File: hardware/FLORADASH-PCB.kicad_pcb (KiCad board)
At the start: 2 copper layers, 101.5 x 58.8 mm, 76 parts, among them IC1 LM66200DRLR, J1 USB_C_Receptacle_USB2.0_16P, J2 Conn_01x04_Pin, J3 Conn_02x04_Top_Bottom, Q1 FS8205, Q2 FS8205, SW1 SW_Push, SW2 SW_Push, U1 TP4056-42-ESOP8, U2 USBLC6-2SC6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

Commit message: Routing structure
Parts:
- BT1: moved to B.Cu
- L2: footprint Inductor_SMD:L_0603_1608Metric -> Inductor_SMD:L_1008_2520Metric
- TP1, TP2, TP3, TP4, TP5, TP6: footprint TestPoint:TestPoint_Pad_D2.5mm -> TestPoint:TestPoint_Pad_D1.0mm
- moved C9 181.0 mm to (104.5, 94.2), turned to -90 degrees
- moved U5 178.8 mm to (107.5, 93.8)
- moved D1 171.9 mm to (115.2, 93.7), turned to 90 degrees
- moved R1 171.7 mm to (113.5, 93.7), turned to -90 degrees
- moved IC1 170.7 mm to (111.5, 93.8), turned to 180 degrees
- moved TP3 170.6 mm to (111.8, 91.2)
- moved R13 122.7 mm to (132.0, 75.7), turned to 180 degrees
- moved Q1 122.4 mm to (116.0, 126.5)
- moved TP2 122.2 mm to (120.2, 106.5)
- moved C7 120.6 mm to (127.2, 79.5), turned to 90 degrees
- moved L2 119.7 mm to (137.5, 79.8), turned to -90 degrees
- moved TP4 118.6 mm to (107.5, 96.2)
- moved Q2 116.1 mm to (111.0, 126.5), turned to 180 degrees
- moved C6 115.3 mm to (139.8, 79.8), turned to 90 degrees
- moved U3 114.9 mm to (110.5, 122.4), turned to 90 degrees
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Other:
- board size 101.5 x 58.8 mm -> 88.8 x 45.5 mm
- copper layers 2 -> 4

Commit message: Added the soil moisture sensor on PCB
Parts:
- added G***: LOGO, SparkFun-Aesthetic:SparkFun_Logo_10mm, F.Cu at (263.2, 88.7)
- added G***: LOGO, SparkFun-Aesthetic:SparkFun_Logo_10mm, B.Cu at (263.2, 100.4)
- added kibuzzard-693B565E: G***, kibuzzard-693B565E, F.Cu at (246.7, 88.5)
- added kibuzzard-693B565E: G***, kibuzzard-693B565E, B.Cu at (246.7, 100.7)
- added kibuzzard-6969377A: G***, kibuzzard-6969377A, F.Cu at (231.0, 94.6)
- added kibuzzard-6969378A: G***, kibuzzard-6969378A, F.Cu at (236.1, 96.8)
- added kibuzzard-69693792: G***, kibuzzard-69693792, F.Cu at (242.4, 96.8)
- added kibuzzard-69693797: G***, kibuzzard-69693797, F.Cu at (248.8, 96.8)
- added kibuzzard-6969379D: G***, kibuzzard-6969379D, F.Cu at (255.1, 96.8)
- added kibuzzard-696937A1: G***, kibuzzard-696937A1, F.Cu at (261.4, 96.8)
- added kibuzzard-696937A5: G***, kibuzzard-696937A5, F.Cu at (267.8, 96.8)
- added kibuzzard-6983799B: G***, kibuzzard-6983799B, B.Cu at (231.6, 94.6)
- added kibuzzard-69837BBB: G***, kibuzzard-69837BBB, B.Cu at (270.3, 93.5)
- added kibuzzard-69837BD1: G***, kibuzzard-69837BD1, B.Cu at (265.3, 93.5)
- added kibuzzard-69837BDA: G***, kibuzzard-69837BDA, B.Cu at (260.3, 93.5)
- added kibuzzard-69837BE0: G***, kibuzzard-69837BE0, B.Cu at (255.3, 93.5)
- added kibuzzard-69837BE5: G***, kibuzzard-69837BE5, B.Cu at (250.3, 93.5)
- added kibuzzard-69837BE9: G***, kibuzzard-69837BE9, B.Cu at (245.3, 93.5)
- added kibuzzard-69837BEE: G***, kibuzzard-69837BEE, B.Cu at (240.3, 93.5)
- added kibuzzard-69837BF5: G***, kibuzzard-69837BF5, B.Cu at (235.3, 93.5)
- moved U6 112.5 mm to (201.4, 19.6)
- moved R18 49.1 mm to (131.2, -51.4)
- moved R10 48.6 mm to (62.4, 42.0), turned to 180 degrees
- moved R11 48.3 mm to (62.4, 43.9), turned to 180 degrees
- moved C5 46.1 mm to (64.8, 42.8), turned to -90 degrees
- moved R9 45.1 mm to (59.2, 41.9)
- moved D5 44.2 mm to (128.0, -51.4)
- moved C12 39.8 mm to (128.8, -54.0), turned to -90 degrees
- moved C11 37.1 mm to (130.4, -54.0), turned to -90 degrees
- moved C10 34.5 mm to (132.0, -54.0), turned to -90 degrees
- moved R21 32.4 mm to (154.6, -52.0), turned to 180 degrees
- moved R20 31.8 mm to (154.6, -53.6), turned to 180 degrees
- moved U8 26.6 mm to (142.9, -49.0)
- moved R17 24.4 mm to (154.6, -46.0)
- moved R15 18.4 mm to (154.6, -44.4)
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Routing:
- added copper zone on B.Cu, net TO_CAP_PLATE
- added copper zone on F.Cu, net TO_CAP_PLATE
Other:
- board size 88.8 x 45.5 mm -> 179.8 x 45.6 mm
- board text added: "Route Out"

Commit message: Placement of the Cap Sense
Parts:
- moved G*** 41.3 mm to (224.9, 104.1)
- moved G*** 41.3 mm to (224.9, 115.8)
- moved kibuzzard-6969377A 41.3 mm to (192.7, 110.0)
- moved kibuzzard-6969378A 41.3 mm to (197.8, 112.2)
- moved kibuzzard-69693792 41.3 mm to (204.1, 112.2)
- moved kibuzzard-69693797 41.3 mm to (210.4, 112.2)
- moved kibuzzard-6969379D 41.3 mm to (216.8, 112.2)
- moved kibuzzard-696937A5 41.3 mm to (229.5, 112.2)
- moved kibuzzard-69837BBB 41.3 mm to (232.0, 108.9)
- moved kibuzzard-69837BD1 41.3 mm to (227.0, 108.9)
- moved kibuzzard-69837BDA 41.3 mm to (222.0, 108.9)
- moved kibuzzard-693B565E 41.3 mm to (208.4, 103.9)
- moved kibuzzard-696937A1 41.3 mm to (223.2, 112.2)
- moved kibuzzard-6983799B 41.3 mm to (193.3, 110.0)
- moved kibuzzard-693B565E 41.3 mm to (208.4, 116.1)
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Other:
- board size 179.8 x 45.6 mm -> 141.4 x 44.3 mm

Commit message: Placement of components on PCB
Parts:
- U6: footprint Connector_PinSocket_2.54mm:PinSocket_1x03_P2.54mm_Vertical -> Connector_PinSocket_2.54mm:PinSocket_1x03_P2.54mm_Horizontal
- moved H3 238.2 mm to (188.2, 88.2)
- moved H4 234.4 mm to (188.4, 133.0)
- moved H1 153.6 mm to (104.2, 88.8)
- moved H2 150.3 mm to (104.2, 133.0)
- moved R9 122.4 mm to (139.6, 134.2), turned to 90 degrees
- moved C16 120.6 mm to (175.8, 105.0)
- moved D4 120.6 mm to (186.7, 106.0)
- moved C15 120.6 mm to (175.8, 106.6)
- moved C13 120.6 mm to (179.4, 109.2)
- moved C14 120.6 mm to (182.6, 109.2)
- moved R14 120.6 mm to (186.6, 104.4)
- moved R16 120.6 mm to (186.7, 107.6)
- moved U7 120.6 mm to (181.2, 105.6)
- moved R10 117.9 mm to (139.8, 131.0), turned to -90 degrees
- moved R11 117.7 mm to (141.6, 131.0), turned to -90 degrees
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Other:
- board size 141.4 x 44.3 mm -> 141.4 x 50.8 mm

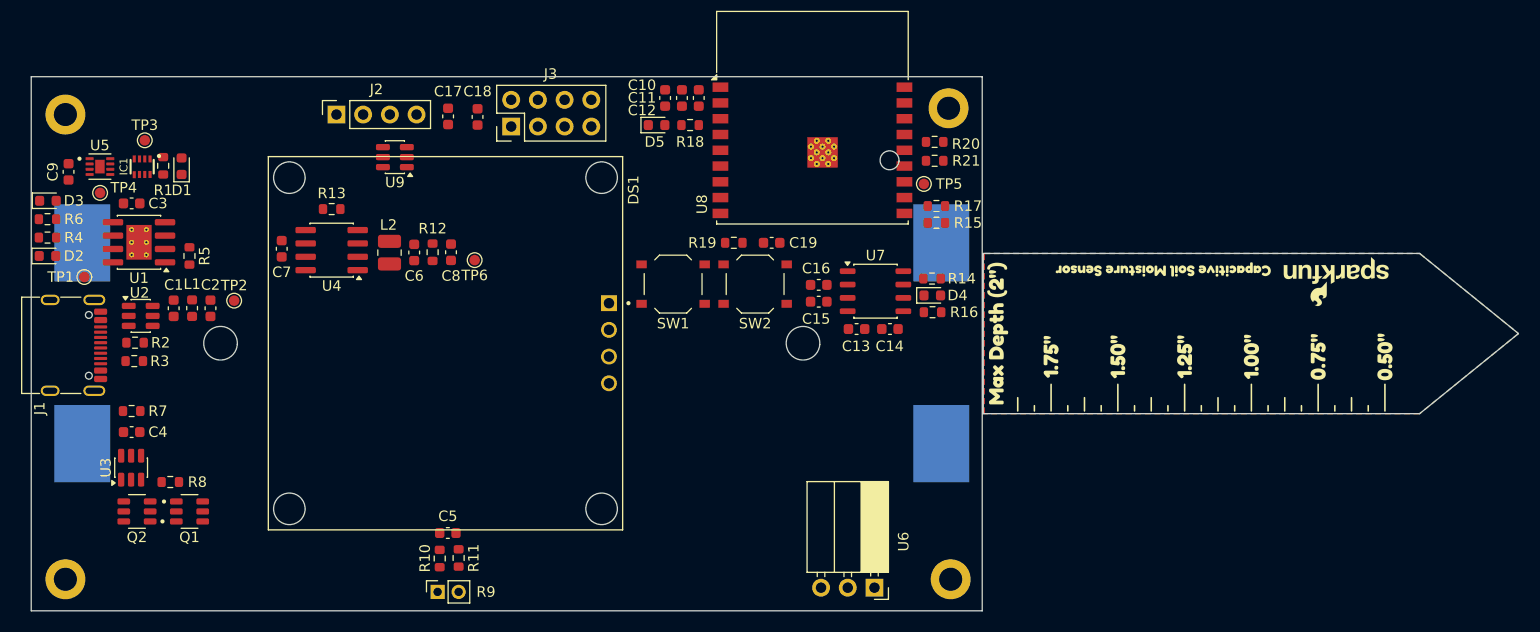
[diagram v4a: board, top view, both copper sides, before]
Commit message: Added ground plane
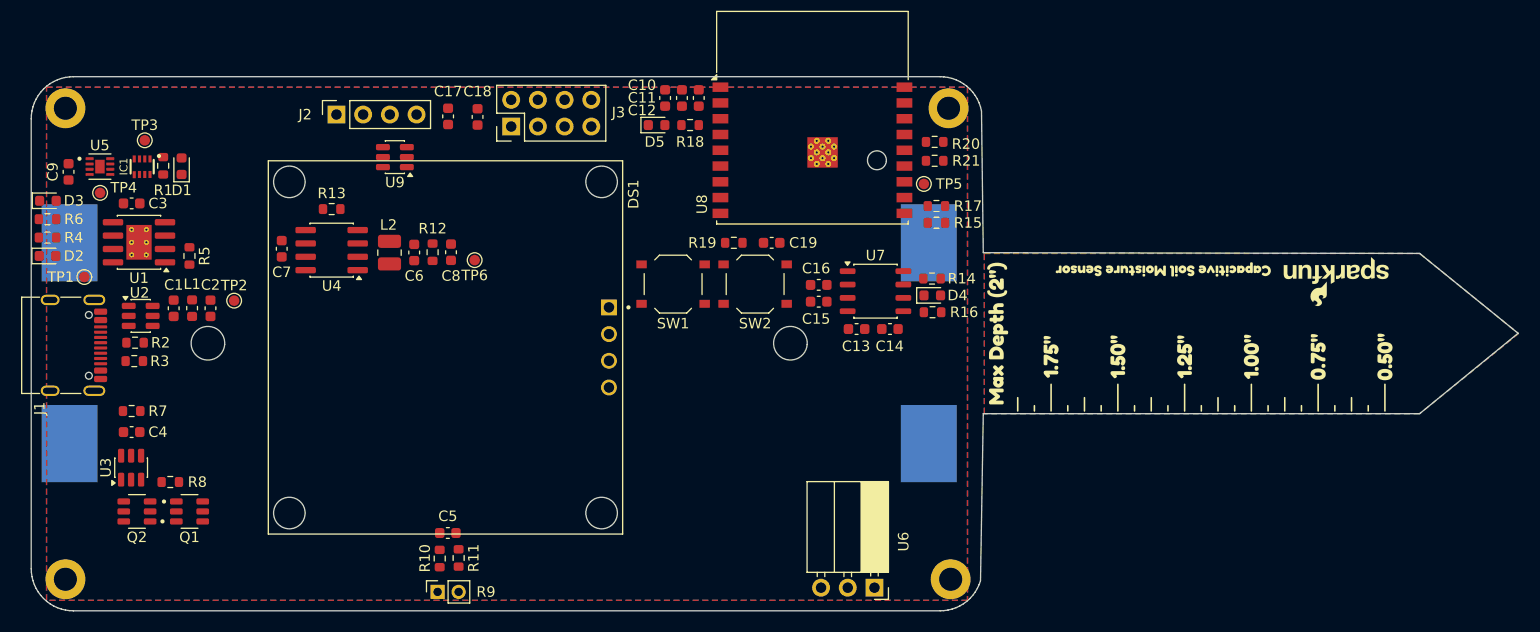
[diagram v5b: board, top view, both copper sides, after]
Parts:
- moved BT1 1.20 mm to (145.5, 110.5)
- moved H1 0.60 mm to (104.2, 88.2)
- moved DS1 0.40 mm to (140.3, 111.0)
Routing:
- added copper zone on B.Cu, net GND
- added copper zone on F.Cu, net GND
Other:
- outline, holes or cut-outs redrawn
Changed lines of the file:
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@@
 		(tags "Through hole socket strip THT 1x04 2.54mm single row")
 		(property "Reference" "J2"
-			(at 2.4 3.8 180)
+			(at 0 -2.98 180)
 			(layer "F.SilkS")
 			(effects
@@
 		(tags "Through hole pin header THT 2x04 2.54mm double row")
 		(property "Reference" "J3"
-			(at 5 3.74 180)
+			(at 1.34 10.2 180)
 			(layer "F.SilkS")
 			(effects
@@
 	(footprint "MountingHole:MountingHole_2.2mm_M2_DIN965_Pad"
 		(layer "F.Cu")
-		(at 104.2 88.8)
+		(at 104.2 88.2)
 		(descr "Mounting Hole 2.2mm, M2, generated by kicad-footprint-generator mountinghole.py")
 		(tags "mountinghole M2 DIN965")
@@
 	(footprint "OLED_128X64_1.3_I2C:LCD_OLED_128X64_1.3_I2C"
 		(layer "F.Cu")
-		(at 140.35 110.55 -90)
+		(at 140.35 110.95 -90)
 		(property "Reference" "DS1"
 			(at -14.575 -17.885 90)
@@
 	(footprint "2-18650:BAT-SMD_BH-18650-B1BA007"
 		(layer "B.Cu")
-		(at 146.655 110.55)
+		(at 145.455 110.55)
 		(property "Reference" "BT1"
 			(at 0 20.980433 0)
@@
 	(gr_poly
 		(pts
-			(xy 242.4 109.63) (xy 233.002 117.25) (xy 191.5 117.25) (xy 191.5 102.01) (xy 233.002 102.01)
+			(xy 100.95 89.2) (xy 100.965221 88.851377) (xy 101.019734 88.456354) (xy 101.113308 88.068721) (xy 101.245012 87.692331)
+			(xy 101.413538 87.330925) (xy 101.617212 86.988095) (xy 101.854008 86.667248) (xy 102.121573 86.371573)
+			(xy 102.417248 86.104008) (xy 102.738095 85.867212) (xy 103.080925 85.663538) (xy 103.442331 85.495012)
+			(xy 103.818721 85.363308) (xy 104.206354 85.269734) (xy 104.601377 85.215221) (xy 104.95 85.2) (xy 187.4 85.2)
+			(xy 187.748623 85.215221) (xy 188.143646 85.269734) (xy 188.531279 85.363308) (xy 188.907669 85.495012)
+			(xy 189.269075 85.663538) (xy 189.611905 85.867212) (xy 189.932752 86.104008) (xy 190.228427 86.371573)
+			(xy 190.495992 86.667248) (xy 190.732788 86.988095) (xy 190.936462 87.330925) (xy 191.104988 87.692331)
+			(xy 191.236692 88.068721) (xy 191.330266 88.456354) (xy 191.499131 101.940638) (xy 233.002 102.01)
+			(xy 242.36615 109.602554) (xy 233.002 117.25) (xy 191.5 117.25) (xy 191.236692 133.131279) (xy 191.104988 133.507669)
+			(xy 190.936462 133.869075) (xy 190.732788 134.211905) (xy 190.495992 134.532752) (xy 190.228427 134.828427)
+			(xy 189.932752 135.095992) (xy 189.611905 135.332788) (xy 189.269075 135.536462) (xy 188.907669 135.704988)
+			(xy 188.531279 135.836692) (xy 188.143646 135.930266) (xy 187.748623 135.984779) (xy 187.4 136) (xy 104.95 136)
+			(xy 104.601377 135.984779) (xy 104.206354 135.930266) (xy 103.818721 135.836692) (xy 103.442331 135.704988)
+			(xy 103.080925 135.536462) (xy 102.738095 135.332788) (xy 102.417248 135.095992) (xy 102.121573 134.828427)
+			(xy 101.854008 134.532752) (xy 101.617212 134.211905) (xy 101.413538 133.869075) (xy 101.245012 133.507669)
+			(xy 101.113308 133.131279) (xy 101.019734 132.743646) (xy 100.965221 132.348623) (xy 100.95 132)
 		)
 		(stroke
-			(width 0.1)
-			(type solid)
-		)
-		(fill no)
-		(layer "Edge.Cuts")
-	)
-	(gr_rect
-		(start 100.95 85.2)
-		(end 191.4 136)
-		(radius 4)
-		(stroke
 			(width 0.05)
 			(type solid)
@@
 			(thermal_gap 0.1778)
 			(thermal_bridge_width 0.1778)
-			(island_removal_mode 0)
+			(island_removal_mode 1)
 		)
 		(polygon
@@
 			)
 		)
+	)
+	(zone
+		(net "GND")
+		(layers "F.Cu" "B.Cu")
+		(name "GND")
+		(hatch edge 0.5)
+		(priority 1)
+		(connect_pads
+			(clearance 0.1778)
+		)
+		(min_thickness 0.25)
+		(fill yes
+			(thermal_gap 0.5)
+			(thermal_bridge_width 0.5)
+			(smoothing fillet)
+			(radius 4)
+			(island_removal_mode 0)
+		)
+		(polygon
+			(pts
+				(xy 102.406646 86.2) (xy 190 86.2) (xy 190 135) (xy 102.406646 135)
+			)
+		)

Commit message: signal routing
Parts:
- moved TP1 5.43 mm to (111.4, 104.8)
- moved TP5 1.75 mm to (187.6, 95.4)
- moved C3 0.92 mm to (109.6, 97.2)
- moved TP3 0.85 mm to (111.8, 90.4)
- moved L1 0.64 mm to (116.8, 106.8)
- moved TP2 0.64 mm to (120.8, 106.1)
- moved C1 0.64 mm to (115.0, 106.8)
- moved C2 0.64 mm to (118.5, 106.8)
- moved TP4 0.50 mm to (107.0, 96.2)
- moved C9 0.28 mm to (104.3, 94.5)
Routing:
- net Bat-: track 0.00 -> 120.2 mm, vias 0 -> 1
- net +3.3V: track 0.00 -> 114.2 mm
- net Bat+: track 0.00 -> 48.1 mm, vias 0 -> 2
- net +5V_FILT: track 0.00 -> 46.8 mm, vias 0 -> 3
- net battery/usb: track 0.00 -> 27.9 mm
- net RST: track 0.00 -> 25.3 mm
- net +5V: track 0.00 -> 24.4 mm
- net GPIO5: track 0.00 -> 22.8 mm, vias 0 -> 1
- net GPIO8: track 0.00 -> 21.2 mm, vias 0 -> 2
- net GPIO6: track 0.00 -> 18.3 mm
- net Net-(U4-FB): track 0.00 -> 16.8 mm
- net GPIO7: track 0.00 -> 16.4 mm, vias 0 -> 1
- net BOOT: track 0.00 -> 13.9 mm
- net Net-(J1-D--PadA7): track 0.00 -> 12.1 mm, vias 0 -> 2
- net Net-(U3-OC): track 0.00 -> 9.79 mm
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
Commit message: Routing PCB v2
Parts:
- removed the G*** at (225.1, 103.8)
- removed the G*** at (225.1, 115.5)
- removed H3: MountingHole, MountingHole:MountingHole_2.2mm_M2_DIN965_Pad
- removed the kibuzzard-693B565E at (208.6, 103.5)
- removed the kibuzzard-693B565E at (208.6, 115.7)
- added G***: LOGO, SparkFun-Aesthetic:SparkFun_Logo_10mm, F.Cu at (228.6, 107.3)
- added G***: LOGO, SparkFun-Aesthetic:SparkFun_Logo_10mm, B.Cu at (228.6, 119.0)
- added kibuzzard-693B565E: G***, kibuzzard-693B565E, F.Cu at (212.0, 107.0)
- added kibuzzard-693B565E: G***, kibuzzard-693B565E, B.Cu at (212.0, 119.2)
- moved SW1 16.6 mm to (165.0, 121.3)
- moved C16 11.9 mm to (180.2, 116.1)
- moved U7 11.8 mm to (185.5, 116.7)
- moved D4 11.8 mm to (190.8, 117.1)
- moved R16 11.8 mm to (190.8, 118.7)
- moved C13 11.8 mm to (183.6, 120.3)
- moved C14 11.8 mm to (186.8, 120.3)
- moved R14 11.8 mm to (190.8, 115.5)
- moved C15 11.8 mm to (180.2, 117.5)
- moved C10 10.4 mm to (167.9, 97.0)
- moved C11 10.4 mm to (166.3, 97.0)
- moved U8 10.4 mm to (178.7, 102.0)
- moved C12 10.4 mm to (164.7, 97.0)
- moved D5 10.4 mm to (163.9, 99.6)
- moved R18 10.4 mm to (167.0, 99.6)
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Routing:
- net SCL: track 4.90 -> 120.6 mm, vias 0 -> 2
- net SDA: track 5.32 -> 114.1 mm, vias 0 -> 2
- net ADC_LUX: track 1.60 -> 66.4 mm, vias 0 -> 2
- net +3.3V: track 114.2 -> 153.9 mm
- net TEMP/HUM: track 0.00 -> 38.6 mm, vias 0 -> 2
- net GPIO10: track 0.00 -> 38.3 mm, vias 0 -> 2
- net RST: track 25.3 -> 35.4 mm, vias 0 -> 2
- net BOOT: track 13.9 -> 22.3 mm
- net GPIO5: track 22.8 -> 29.6 mm
- net GPIO8: track 21.2 -> 25.8 mm, vias 2 -> 1
- net GPIO6: track 18.3 -> 22.9 mm
- net Bat-: track 120.2 -> 124.7 mm, vias 1 -> 2
- net GPIO7: track 16.4 -> 19.6 mm
- net Net-(R10-Pad2): track 4.22 -> 6.62 mm
- net Net-(U8-IO21/TXD): track 0.00 -> 2.20 mm
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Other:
- board size 141.4 x 50.8 mm -> 139.5 x 50.9 mm

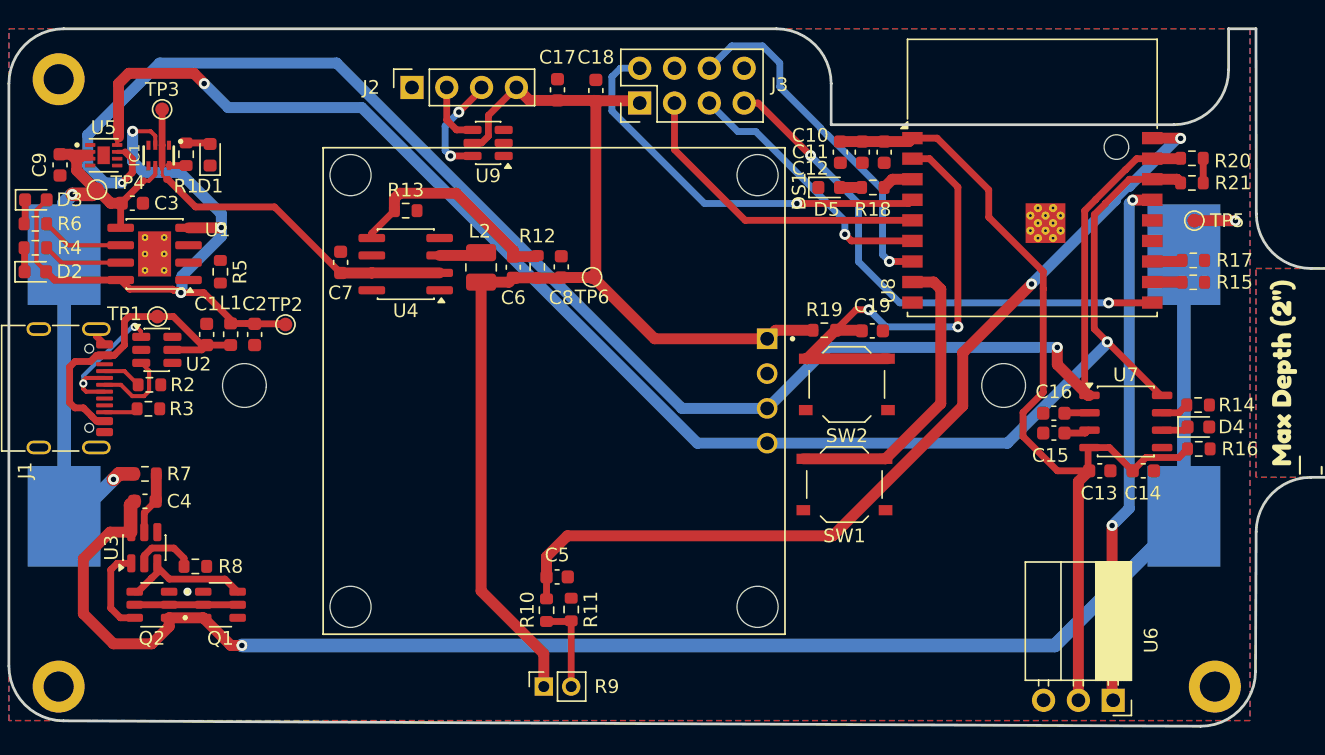
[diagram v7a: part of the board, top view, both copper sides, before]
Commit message: new calculated signals track width
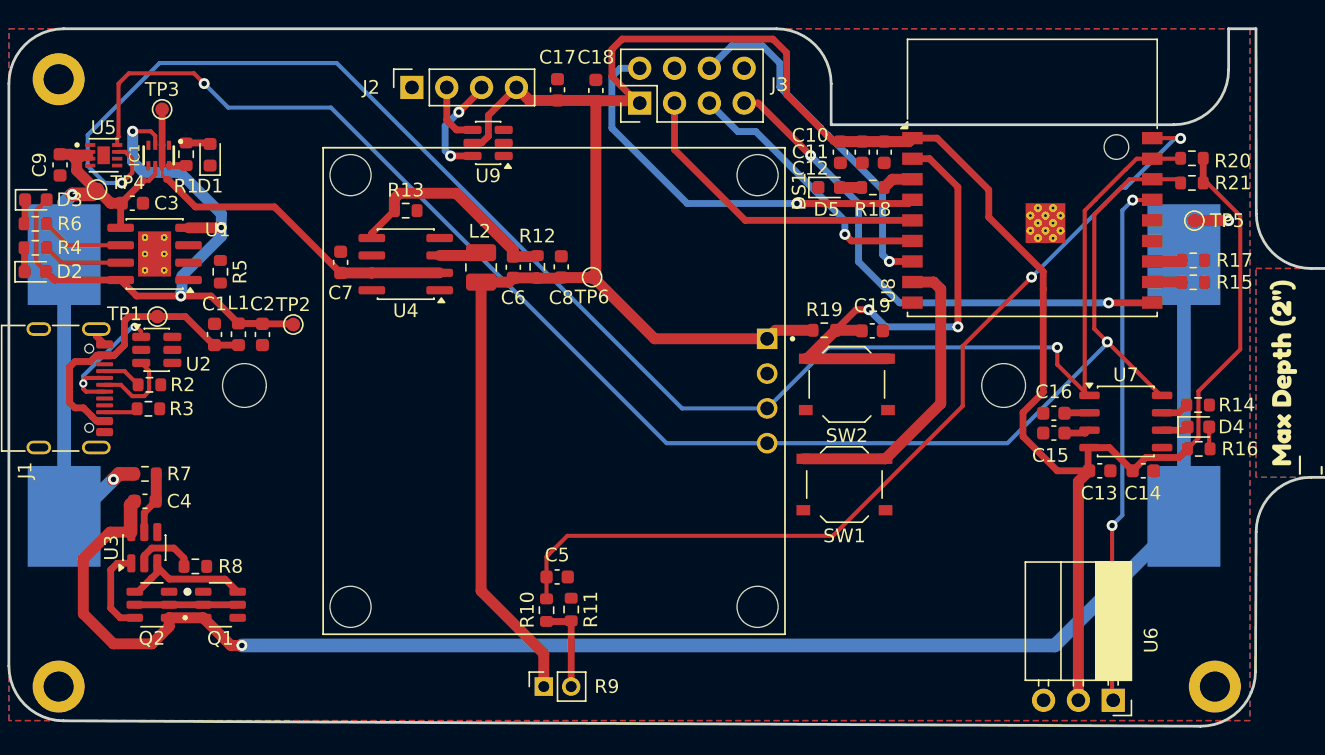
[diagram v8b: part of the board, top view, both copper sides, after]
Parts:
- moved C1 0.57 mm to (119.0, 110.3)
- moved C2 0.57 mm to (122.5, 110.3)
- moved L1 0.57 mm to (120.8, 110.3)
- moved TP2 0.57 mm to (124.8, 109.6)
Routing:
- net +3.3V: track 153.9 -> 202.9 mm
- net +5V: track 23.5 -> 21.5 mm
- net Net-(D4-A): track 0.00 -> 1.63 mm
- net Bat-: track 124.7 -> 123.7 mm
- net +5V_FILT: track 47.0 -> 47.8 mm
- net GPIO5: track 29.6 -> 30.4 mm
